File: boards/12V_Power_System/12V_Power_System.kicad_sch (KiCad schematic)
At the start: 5 parts

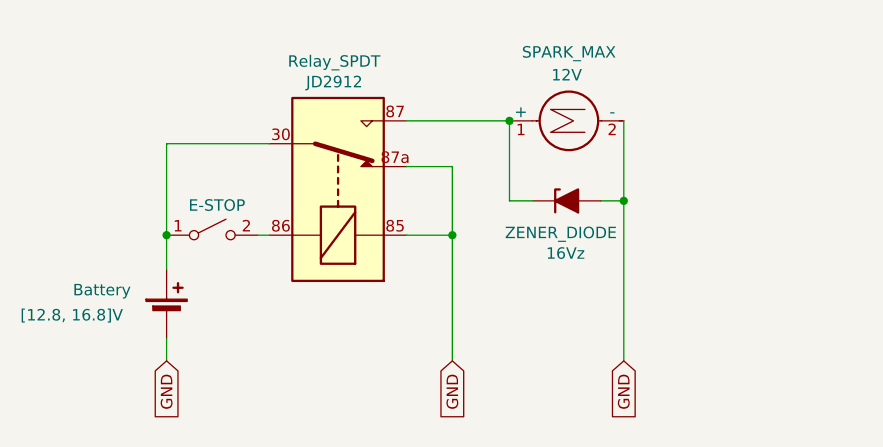
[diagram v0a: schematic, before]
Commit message: improved schematic and starting pcb
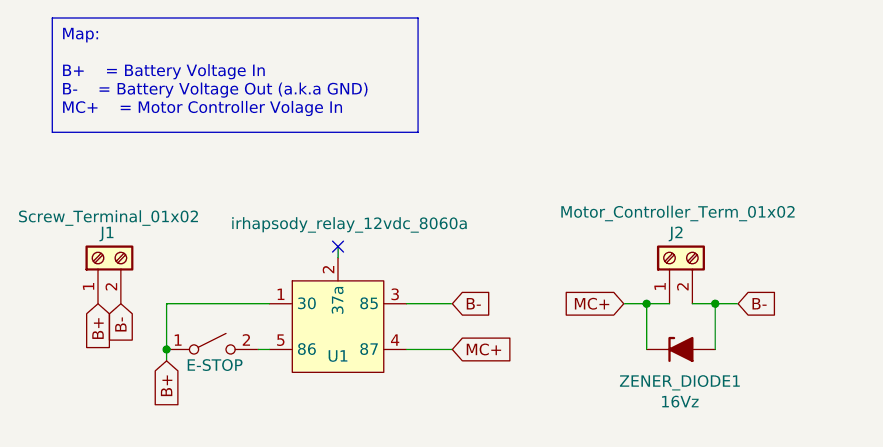
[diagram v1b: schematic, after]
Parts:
- removed Battery: [12.8, 16.8]V, symbol Device:Battery_Cell
- removed JD2912: Relay_SPDT, symbol Relay:Relay_SPDT
- removed SPARK_MAX: 12V, symbol Motor:Motor_DC
- added J1: Screw_Terminal_01x02, TerminalBlock:TerminalBlock_Xinya_XY308-2.54-2P_1x02_P2.54mm_Horizontal, symbol Connector:Screw_Terminal_01x02
- added J2: Motor_Controller_Term_01x02, TerminalBlock:TerminalBlock_Xinya_XY308-2.54-2P_1x02_P2.54mm_Horizontal, symbol Connector:Screw_Terminal_01x02
- added U1: irhapsody_relay_12vdc_8060a, IRIS:IRhapsody Relay 12VDC 8060A, symbol irhapsody_relay_12vdc_8060a:Irhapsody_Relay_12VDC_80/60A
- ZENER_DIODE1: renamed from ZENER_DIODE; footprint (none) -> Diode_THT:D_DO-34_SOD68_P10.16mm_Horizontal
- renumbered E-STOP to E-STOP1
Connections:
- net B+: now reaches E-STOP1.1 (A)
- net B+: now also J1.1 (Pin_1), U1.1 (30)
- net at E-STOP1.2 (B): now also U1.5 (86)
- net MC+: now reaches ZENER_DIODE1.1 (K)
- net MC+: now also J2.1 (Pin_1), U1.4 (87)
- net GND renamed B-
- net B-: now also J1.2 (Pin_2), J2.2 (Pin_2), U1.3 (85)
- no-connect marks 0 -> 1
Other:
- title: 12 Power System -> 12V Power System
- moved on the sheet: ZENER_DIODE1

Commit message: make schematic better again
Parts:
- E-STOP1: value E-STOP -> E-STOP NC
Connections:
- net B-: now also U1.4 (85); no longer U1.3 (85)
- net MC+: now also U1.3 (87); no longer U1.4 (87)
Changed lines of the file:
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@@
+	(wire
+		(pts
+			(xy 119.38 57.15) (xy 116.84 57.15)
+		)
+		(stroke
+			(width 0)
+			(type default)
+		)
+	)
+	(wire
+		(pts
+			(xy 63.5 57.15) (xy 63.5 62.23)
+		)
+		(stroke
+			(width 0)
+			(type default)
+		)
+	)
+	(wire
+		(pts
+			(xy 124.46 57.15) (xy 124.46 62.23)
+		)
+		(stroke
+			(width 0)
+			(type default)
+		)
+	)
+	(wire
+		(pts
+			(xy 90.17 57.15) (xy 95.25 57.15)
+		)
+		(stroke
+			(width 0)
+			(type default)
+		)
+	)
+	(wire
+		(pts
+			(xy 124.46 57.15) (xy 127 57.15)
+		)
+		(stroke
+			(width 0)
+			(type default)
+		)
+	)
+	(wire
+		(pts
+			(xy 114.3 57.15) (xy 116.84 57.15)
+		)
+		(stroke
+			(width 0)
+			(type default)
+		)
+	)
+	(wire
+		(pts
+			(xy 63.5 63.5) (xy 63.5 62.23)
+		)
+		(stroke
+			(width 0)
+			(type default)
+		)
+	)
+	(wire
+		(pts
+			(xy 63.5 57.15) (xy 74.93 57.15)
+		)
+		(stroke
+			(width 0)
+			(type default)
+		)
+	)
 	(wire
 		(pts
 			(xy 90.17 62.23) (xy 95.25 62.23)
-		)
-		(stroke
-			(width 0)
-			(type default)
-		)
-	)
-	(wire
-		(pts
-			(xy 119.38 57.15) (xy 116.84 57.15)
-		)
-		(stroke
-			(width 0)
-			(type default)
-		)
-	)
-	(wire
-		(pts
-			(xy 63.5 57.15) (xy 63.5 62.23)
-		)
-		(stroke
-			(width 0)
-			(type default)
-		)
-	)
-	(wire
-		(pts
-			(xy 124.46 57.15) (xy 124.46 62.23)
-		)
-		(stroke
-			(width 0)
-			(type default)
-		)
-	)
-	(wire
-		(pts
-			(xy 124.46 57.15) (xy 127 57.15)
-		)
-		(stroke
-			(width 0)
-			(type default)
-		)
-	)
-	(wire
-		(pts
-			(xy 114.3 57.15) (xy 116.84 57.15)
-		)
-		(stroke
-			(width 0)
-			(type default)
-		)
-	)
-	(wire
-		(pts
-			(xy 63.5 63.5) (xy 63.5 62.23)
-		)
-		(stroke
-			(width 0)
-			(type default)
-		)
-	)
-	(wire
-		(pts
-			(xy 90.17 57.15) (xy 95.25 57.15)
-		)
-		(stroke
-			(width 0)
-			(type default)
-		)
-	)
-	(wire
-		(pts
-			(xy 63.5 57.15) (xy 74.93 57.15)
 		)
 		(stroke
@@
 	(global_label "B-"
 		(shape input)
+		(at 95.25 62.23 0)
+		(fields_autoplaced yes)
+		(effects
+			(font
+				(size 1.27 1.27)
+			)
+			(justify left)
+		)
+		(property "Intersheetrefs" "${INTERSHEET_REFS}"
+			(at 101.0776 62.23 0)
+			(effects
+				(font
+					(size 1.27 1.27)
+				)
+				(justify left)
+				(hide yes)
+			)
+		)
+	)
+	(global_label "MC+"
+		(shape input)
+		(at 114.3 57.15 180)
+		(fields_autoplaced yes)
+		(effects
+			(font
+				(size 1.27 1.27)
+			)
+			(justify right)
+		)
+		(property "Intersheetrefs" "${INTERSHEET_REFS}"
+			(at 107.021 57.15 0)
+			(effects
+				(font
+					(size 1.27 1.27)
+				)
+				(justify right)
+				(hide yes)
+			)
+		)
+	)
+	(global_label "MC+"
+		(shape input)
 		(at 95.25 57.15 0)
 		(fields_autoplaced yes)
@@
 		)
 		(property "Intersheetrefs" "${INTERSHEET_REFS}"
-			(at 101.0776 57.15 0)
-			(effects
-				(font
-					(size 1.27 1.27)
-				)
-				(justify left)
-				(hide yes)
-			)
-		)
-	)
-	(global_label "MC+"
-		(shape input)
-		(at 114.3 57.15 180)
-		(fields_autoplaced yes)
-		(effects
-			(font
-				(size 1.27 1.27)
-			)
-			(justify right)
-		)
-		(property "Intersheetrefs" "${INTERSHEET_REFS}"
-			(at 107.021 57.15 0)
-			(effects
-				(font
-					(size 1.27 1.27)
-				)
-				(justify right)
-				(hide yes)
-			)
-		)
-	)
-	(global_label "MC+"
-		(shape input)
-		(at 95.25 62.23 0)
-		(fields_autoplaced yes)
-		(effects
-			(font
-				(size 1.27 1.27)
-			)
-			(justify left)
-		)
-		(property "Intersheetrefs" "${INTERSHEET_REFS}"
-			(at 102.529 62.23 0)
+			(at 102.529 57.15 0)
 			(effects
 				(font
@@
 			)
 		)
-		(property "Value" "E-STOP"
-			(at 68.834 64.008 0)
-			(effects
-				(font
+		(property "Value" "E-STOP NC"
+			(at 70.612 63.754 0)
+			(effects
+				(font

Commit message: footprints
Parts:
- added E-STOP2, E-STOP3, E-STOP4: E-STOP NC, symbol Switch:SW_DPST_x2
- added E-STOP5: E-STOP NC, REAAAL:E-Stop, symbol Switch:SW_DPST_x2
- added J10: Motor_Controller_5_Term_01x02, TerminalBlock:TerminalBlock_Xinya_XY308-2.54-2P_1x02_P2.54mm_Horizontal, symbol Connector:Screw_Terminal_01x02
- added J4: Motor_Controller_2_Term_01x02, TerminalBlock:TerminalBlock_Xinya_XY308-2.54-2P_1x02_P2.54mm_Horizontal, symbol Connector:Screw_Terminal_01x02
- added J6: Motor_Controller_1_Term_01x02, TerminalBlock:TerminalBlock_Xinya_XY308-2.54-2P_1x02_P2.54mm_Horizontal, symbol Connector:Screw_Terminal_01x02
- added J8: Motor_Controller_4_Term_01x02, TerminalBlock:TerminalBlock_Xinya_XY308-2.54-2P_1x02_P2.54mm_Horizontal, symbol Connector:Screw_Terminal_01x02
- added U2: irhapsody_relay_12vdc_8060a_2, REAAAL:IRhapsody Relay 12VDC 8060A, symbol irhapsody_relay_12vdc_8060a:Irhapsody_Relay_12VDC_80/60A
- added U3: irhapsody_relay_12vdc_8060a_3, REAAAL:IRhapsody Relay 12VDC 8060A, symbol irhapsody_relay_12vdc_8060a:Irhapsody_Relay_12VDC_80/60A
- added U4: irhapsody_relay_12vdc_8060a_4, REAAAL:IRhapsody Relay 12VDC 8060A, symbol irhapsody_relay_12vdc_8060a:Irhapsody_Relay_12VDC_80/60A
- added U5: irhapsody_relay_12vdc_8060a_5, REAAAL:IRhapsody Relay 12VDC 8060A, symbol irhapsody_relay_12vdc_8060a:Irhapsody_Relay_12VDC_80/60A
- added ZENER_DIODE2, ZENER_DIODE3, ZENER_DIODE4, ZENER_DIODE5: 16Vz, Diode_THT:D_DO-34_SOD68_P10.16mm_Horizontal, symbol Device:D_Zener_Filled
- J2: value Motor_Controller_Term_01x02 -> Motor_Controller_1_Term_01x02
- U1: value irhapsody_relay_12vdc_8060a -> irhapsody_relay_12vdc_8060a_1; footprint IRIS:IRhapsody Relay 12VDC 8060A -> REAAAL:IRhapsody Relay 12VDC 8060A
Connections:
- net B+: now also E-STOP2.1 (A), E-STOP3.1 (A), E-STOP4.1 (A), E-STOP5.1 (A), U2.1 (30), U3.1 (30), U4.1 (30), U5.1 (30)
- net B-: now also J10.2 (Pin_2), J4.2 (Pin_2), J6.2 (Pin_2), J8.2 (Pin_2), U2.4 (85), U3.4 (85), U4.4 (85), U5.4 (85), ZENER_DIODE2.2 (A), ZENER_DIODE3.2 (A), ZENER_DIODE4.2 (A), ZENER_DIODE5.2 (A)
- net MC+ renamed MC_1+
- new net: E-STOP3.2 (B), U3.5 (86)
- new net: E-STOP2.2 (B), U2.5 (86)
- new net: E-STOP4.2 (B), U4.5 (86)
- new net: E-STOP5.2 (B), U5.5 (86)
- new net MC_2+: J4.1 (Pin_1), U2.3 (87), ZENER_DIODE2.1 (K)
- new net MC_3+: J6.1 (Pin_1), U3.3 (87), ZENER_DIODE3.1 (K)
- new net MC_4+: J8.1 (Pin_1), U4.3 (87), ZENER_DIODE4.1 (K)
- new net MC_5+: J10.1 (Pin_1), U5.3 (87), ZENER_DIODE5.1 (K)
- no-connect marks 1 -> 5

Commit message: updated schematic
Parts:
- removed E-STOP1, E-STOP2, E-STOP3, E-STOP4: E-STOP NC, symbol Switch:SW_DPST_x2
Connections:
- net at U3.5 (86): now also E-STOP5.2 (B), U1.5 (86), U2.5 (86), U4.5 (86), U5.5 (86)
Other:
- moved on the sheet: J1

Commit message: updated board layout
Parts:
- removed J1: Screw_Terminal_01x02, TerminalBlock:TerminalBlock_Xinya_XY308-2.54-2P_1x02_P2.54mm_Horizontal, symbol Connector:Screw_Terminal_01x02
- removed J10: Motor_Controller_5_Term_01x02, TerminalBlock:TerminalBlock_Xinya_XY308-2.54-2P_1x02_P2.54mm_Horizontal, symbol Connector:Screw_Terminal_01x02
- removed J2, J6: Motor_Controller_1_Term_01x02, TerminalBlock:TerminalBlock_Xinya_XY308-2.54-2P_1x02_P2.54mm_Horizontal, symbol Connector:Screw_Terminal_01x02
- removed J4: Motor_Controller_2_Term_01x02, TerminalBlock:TerminalBlock_Xinya_XY308-2.54-2P_1x02_P2.54mm_Horizontal, symbol Connector:Screw_Terminal_01x02
- removed J8: Motor_Controller_4_Term_01x02, TerminalBlock:TerminalBlock_Xinya_XY308-2.54-2P_1x02_P2.54mm_Horizontal, symbol Connector:Screw_Terminal_01x02
- added J1, J2, J3, J4, J5, J6: 1986660-2, REAAAL:TE_1986660-2, symbol 1986660-2:1986660-2
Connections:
- net B+: now also J1.1_1 (1)
- net B-: now also J1.2_1 (2), J2.2_1 (2), J3.2_1 (2), J4.2_1 (2), J5.2_1 (2), J6.2_1 (2)
- net MC_1+: now also J2.1_1 (1)
- net MC_2+: now also J3.1_1 (1)
- net MC_3+: now also J4.1_1 (1)
- net MC_4+: now also J5.1_1 (1)
- net MC_5+: now also J6.1_1 (1)

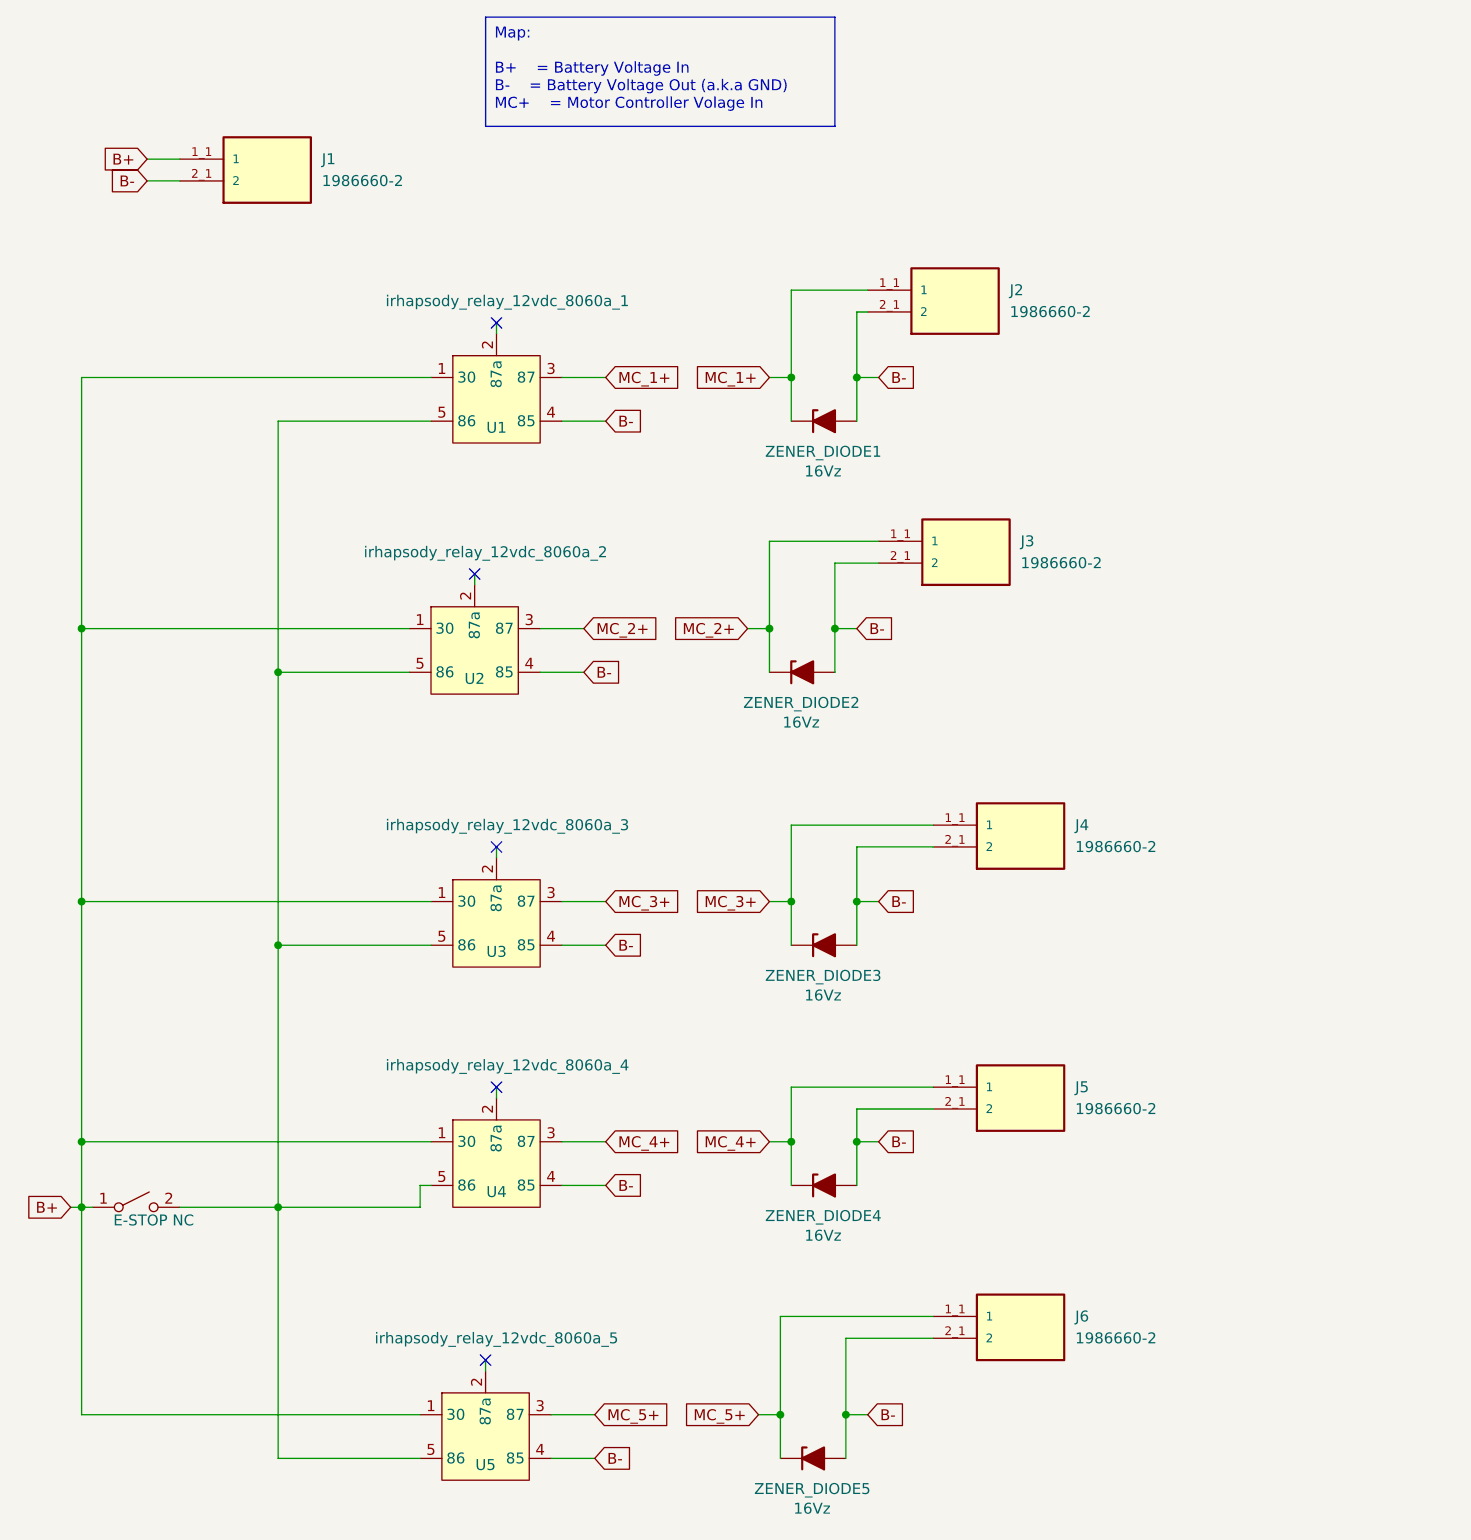
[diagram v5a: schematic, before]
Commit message: tidied up the schematic
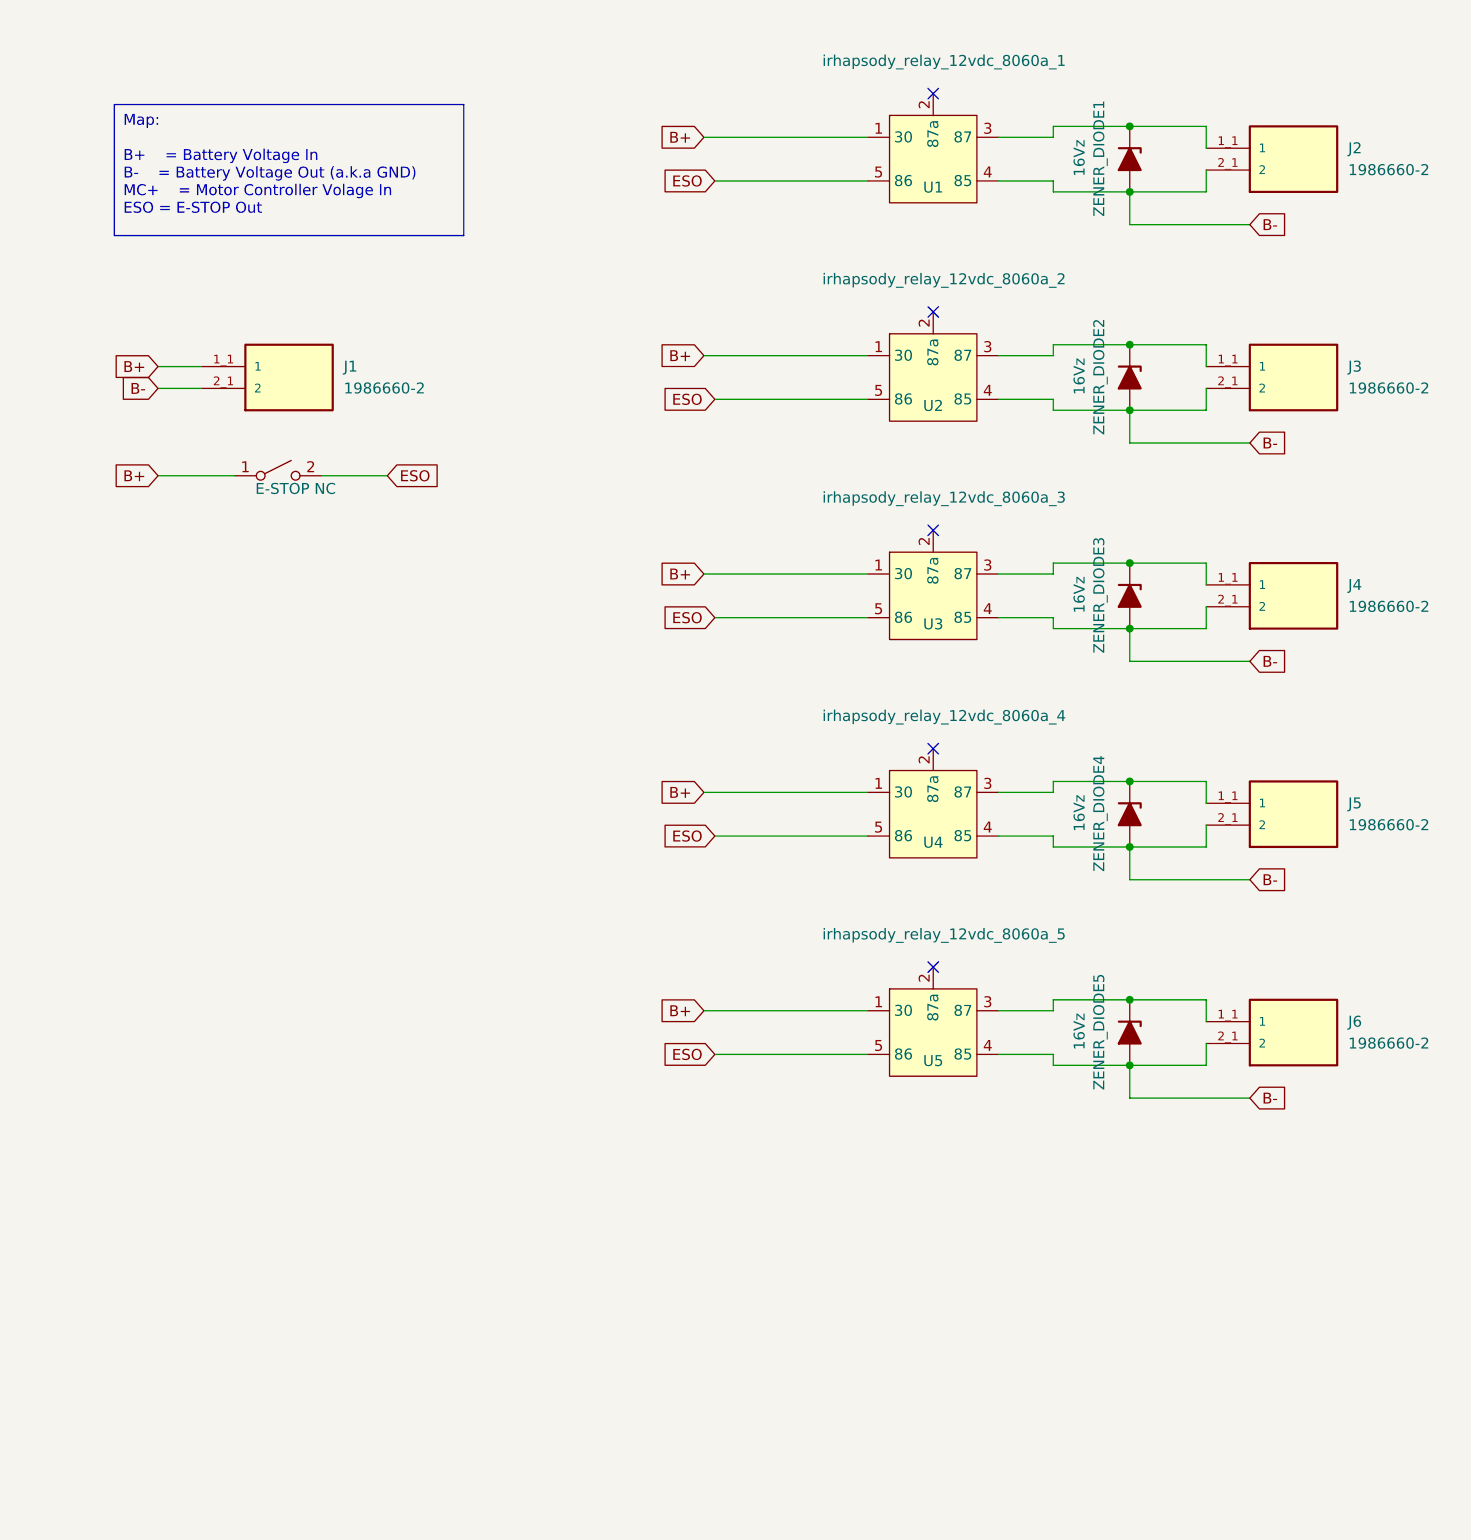
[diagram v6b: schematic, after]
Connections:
- net ESO: now reaches E-STOP5.2 (B), U1.5 (86), U2.5 (86), U3.5 (86), U4.5 (86), U5.5 (86)
- net MC_1+: no longer names the net of J2.1_1 (1), U1.3 (87), ZENER_DIODE1.1 (K)
- net MC_2+: no longer names the net of J3.1_1 (1), U2.3 (87), ZENER_DIODE2.1 (K)
- net MC_3+: no longer names the net of J4.1_1 (1), U3.3 (87), ZENER_DIODE3.1 (K)
- net MC_4+: no longer names the net of J5.1_1 (1), U4.3 (87), ZENER_DIODE4.1 (K)
- net MC_5+: no longer names the net of J6.1_1 (1), U5.3 (87), ZENER_DIODE5.1 (K)
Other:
- moved on the sheet: J1, J2, U1
